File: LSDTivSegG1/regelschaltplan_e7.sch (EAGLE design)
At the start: 89 parts, among them IC1 LF33AB, IC3 MAX232, IC4 MEGA32-P, Q2 BS170, Q3 BS170, Q4 BS170, Q5 BS170, Q6 BS170, Q7 BS170, Q8 BS170

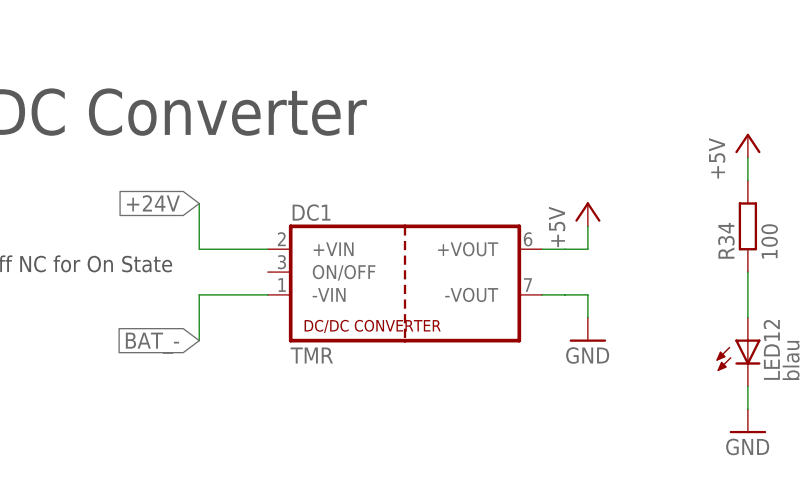
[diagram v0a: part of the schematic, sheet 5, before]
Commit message: edit  regelschaltplan_e7 bauteil fixed
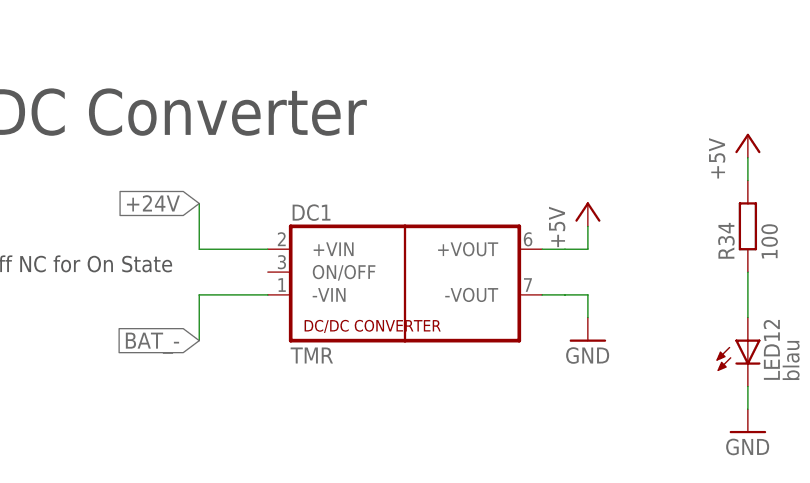
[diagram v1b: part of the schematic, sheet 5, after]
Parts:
- DC1: device traco_tmr:TMR -> regelschaltplan_e7:TMR
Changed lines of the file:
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@@
 <?xml version="1.0" encoding="utf-8"?>
 <!DOCTYPE eagle SYSTEM "eagle.dtd">
-<eagle version="7.7.0">
+<eagle version="6.5.0">
 <drawing>
 <settings>
@@
 <part name="R27" library="rcl" deviceset="R-EU_" device="0207/10" value="330"/>
 <part name="FRAME8" library="frames" deviceset="FRAME_A_L" device=""/>
-<part name="DC1" library="traco_tmr" deviceset="TMR" device=""/>
+<part name="DC1" library="regelschaltplan_e7" deviceset="TMR" device=""/>
 <part name="LED12" library="led" deviceset="LED" device="3MM" value="blau"/>
 <part name="R34" library="rcl" deviceset="R-EU_" device="0207/10" value="100"/>
